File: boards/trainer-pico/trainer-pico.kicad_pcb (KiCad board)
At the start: 2 copper layers, 132.1 x 99.1 mm, 38 parts, among them J1 Conn_01x08_Pin, J10 Conn_01x04_Socket, J11 Conn_01x17_Pin, J12 Conn_01x17_Socket, J13 Conn_01x17_Socket, J14 Conn_01x17_Pin, J15 Barrel_Jack_Switch, J16 Conn_01x04_Pin, J17 Conn_01x04_Pin, J18 Conn_01x04_Pin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

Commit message: 改番
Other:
- board text added: "trainer-pico v1.1"
- board text removed: "trainer-pico v1.0"
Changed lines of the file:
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@@
 		)
 	)
-	(gr_text "trainer-pico v1.0"
+	(gr_text "trainer-pico v1.1"
 		(at 63.5 144.78 0)
 		(layer "F.SilkS")

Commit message: 配置の修正とピンアサインの刻印の追加
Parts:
- moved J10 7.62 mm to (119.4, 111.8)
- moved J5 7.62 mm to (111.8, 111.8)
- moved J4 5.08 mm to (111.8, 96.5)
- moved J9 5.08 mm to (119.4, 96.5)
- moved J3 2.54 mm to (111.8, 76.2)
- moved J8 2.54 mm to (119.4, 76.2)
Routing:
- net /UART_PICO_RX: track 63.1 -> 56.9 mm
- net /UART_PICO_TX: track 63.1 -> 56.9 mm
- net /I2C_SCL: track 74.1 -> 69.8 mm
- net /I2C_SDA: track 72.3 -> 68.0 mm
- net /SPI_MISO: track 65.6 -> 66.7 mm
- net GND: vias 214 -> 207
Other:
- board text added: "I2C0"
- board text added: "SPI1"
- board text added: "SPI1_MISO - GP8 SPI1_MOSI - GP9 SPI1_SCK - GP10 SPI1_CS - GP11 I2C0_SDA - GP21 I2C0_SCL - GP20 UART0_RX - GP17 UART0_TX - GP16"
- board text added: "UART0"
- board text removed: "I2C"
- board text removed: "SPI"
- board text removed: "UART"

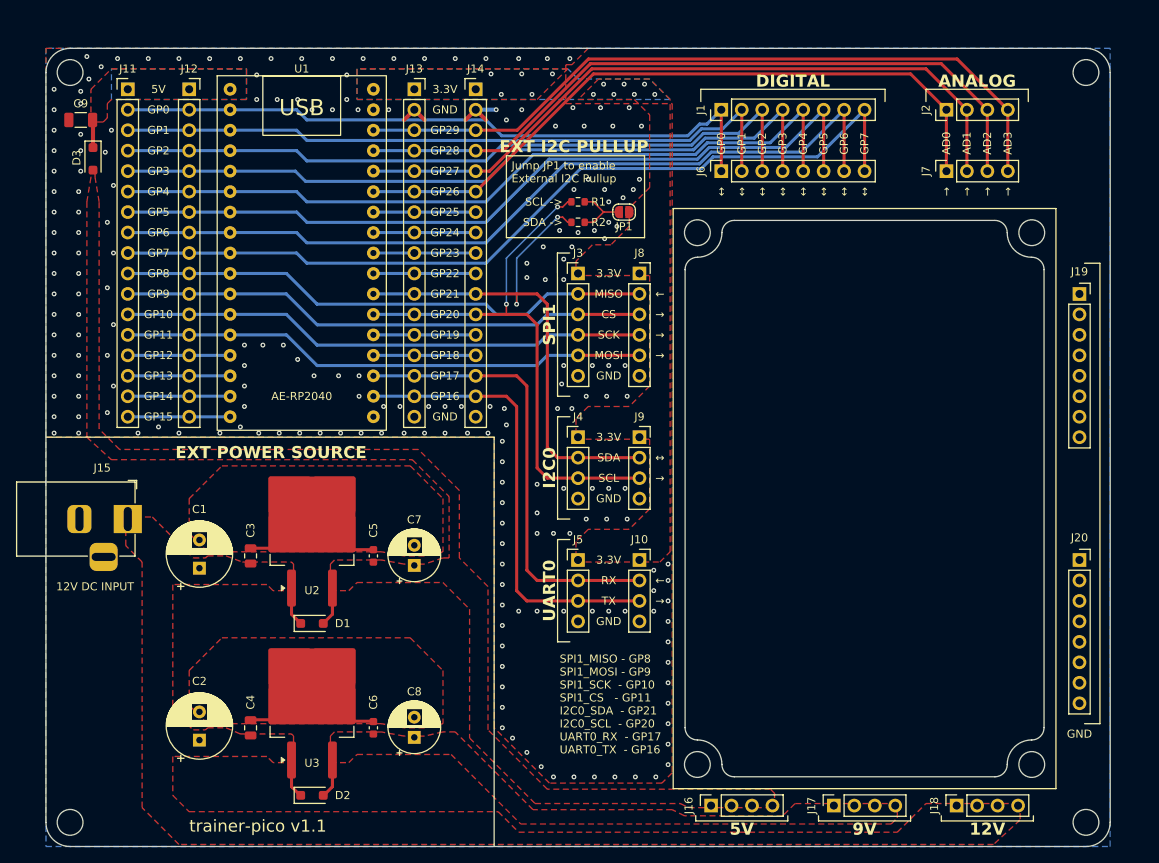
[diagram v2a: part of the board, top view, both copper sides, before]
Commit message: サブ基板の固定方法を変更
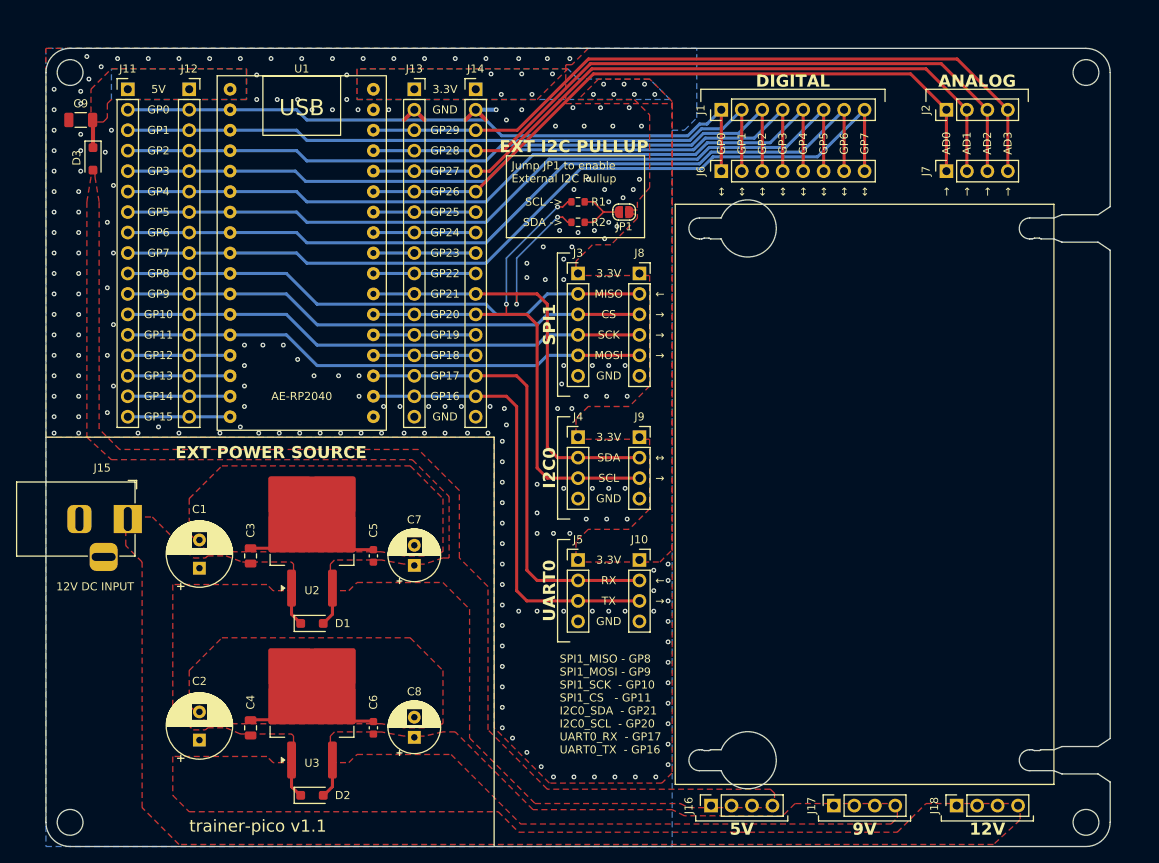
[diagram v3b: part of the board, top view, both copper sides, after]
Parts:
- removed J19, J20: Conn_01x08_Pin, Connector_PinSocket_2.54mm:PinSocket_1x08_P2.54mm_Vertical
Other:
- outline, holes or cut-outs redrawn

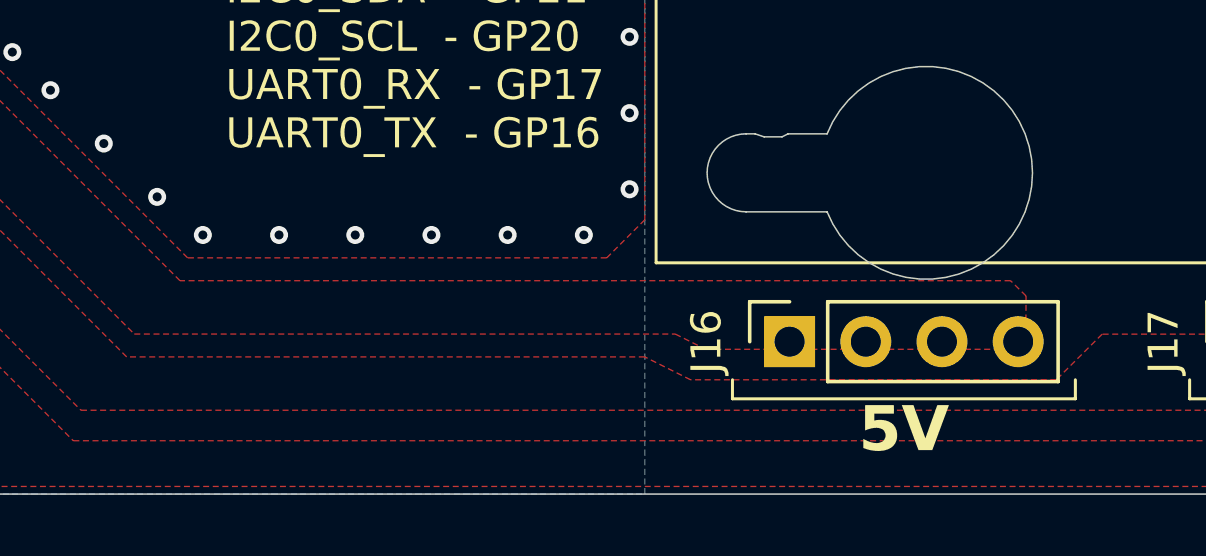
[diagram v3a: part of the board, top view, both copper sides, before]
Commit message: ベタ形状変更
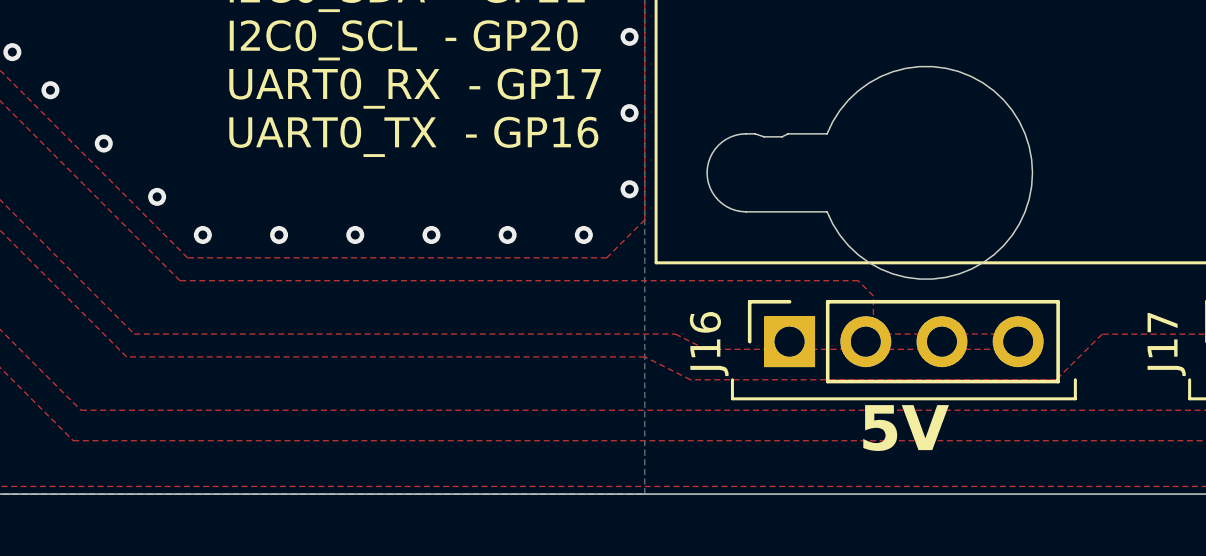
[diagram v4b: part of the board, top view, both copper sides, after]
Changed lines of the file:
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@@
-		(polygon
-			(pts
-				(xy 133.604 140.97) (xy 133.604 141.986) (xy 135.636 141.986) (xy 135.636 140.97)
-			)
-		)
-	)
-	(zone
-		(net 0)
-		(net_name "")
-		(layer "F.Cu")
-		(hatch edge 0.5)
-		(connect_pads
-			(clearance 0)
-		)
-		(min_thickness 0.25)
-		(filled_areas_thickness no)
-		(keepout
-			(tracks allowed)
-			(vias allowed)
-			(pads allowed)
-			(copperpour not_allowed)
-			(footprints allowed)
-		)
-		(fill
-			(thermal_gap 0.5)
-			(thermal_bridge_width 0.5)
-		)
 		(polygon
 			(pts
@@
 				(xy 81.026 115.57) (xy 83.312 115.57) (xy 84.328 114.554) (xy 94.996 114.554) (xy 98.298 117.856)
 				(xy 98.298 133.858) (xy 106.426 141.986) (xy 124.46 141.986) (xy 125.476 142.494) (xy 136.144 142.494)
-				(xy 136.152 140.716) (xy 135.636 140.208) (xy 107.95 140.208) (xy 100.584 132.842) (xy 100.584 115.062)
-				(xy 97.028 111.506) (xy 97.028 103.124) (xy 91.948 98.044) (xy 54.864 98.044) (xy 52.324 95.504)
-				(xy 52.324 67.31) (xy 51.816 64.262) (xy 51.816 63.633) (xy 51.816 63.004) (xy 51.308 63.004) (xy 51.308 64.262)
-				(xy 50.8 67.31) (xy 50.8 96.52) (xy 53.848 99.314) (xy 91.186 99.314) (xy 95.758 103.886) (xy 95.758 111.506)
-				(xy 94.996 111.506) (xy 92.71 112.268) (xy 90.17 112.268) (xy 87.376 111.76) (xy 81.534 111.76)
-				(xy 81.026 112.268)
+				(xy 136.144 141.986) (xy 131.064 141.986) (xy 131.064 140.716) (xy 130.556 140.208) (xy 107.95 140.208)
+				(xy 100.584 132.842) (xy 100.584 115.062) (xy 97.028 111.506) (xy 97.028 103.124) (xy 91.948 98.044)
+				(xy 54.864 98.044) (xy 52.324 95.504) (xy 52.324 67.31) (xy 51.816 64.262) (xy 51.816 63.633) (xy 51.816 63.004)
+				(xy 51.308 63.004) (xy 51.308 64.262) (xy 50.8 67.31) (xy 50.8 96.52) (xy 53.848 99.314) (xy 91.186 99.314)
+				(xy 95.758 103.886) (xy 95.758 111.506) (xy 94.996 111.506) (xy 92.71 112.268) (xy 90.17 112.268)
+				(xy 87.376 111.76) (xy 81.534 111.76) (xy 81.026 112.268)
 			)
 		)
@@
 		(polygon
 			(pts
-				(xy 131.064 140.97) (xy 131.064 141.986) (xy 133.096 141.986) (xy 133.096 140.97)
-			)
-		)
-	)
-	(zone
-		(net 0)
-		(net_name "")
-		(layer "F.Cu")
-		(hatch edge 0.5)
-		(connect_pads
-			(clearance 0)
-		)
-		(min_thickness 0.25)
-		(filled_areas_thickness no)
-		(keepout
-			(tracks allowed)
-			(vias allowed)
-			(pads allowed)
-			(copperpour not_allowed)
-			(footprints allowed)
-		)
-		(fill
-			(thermal_gap 0.5)
-			(thermal_bridge_width 0.5)
-		)
-		(polygon
-			(pts
 				(xy 111.252 93.726) (xy 109.22 93.726) (xy 108.458 92.964) (xy 108.458 97.536) (xy 109.474 98.552)
 				(xy 110.49 98.552) (xy 110.49 103.886) (xy 113.03 103.886) (xy 113.03 96.774) (xy 111.252 96.774)
@@
 			)
 		)
-	)
-	(zone
-		(net 0)
-		(net_name "")
-		(layers "F&B.Cu" "Edge.Cuts")
-		(hatch edge 0.5)
-		(connect_pads
-			(clearance 0)
-		)
-		(min_thickness 0.25)
-		(filled_areas_thickness no)
-		(keepout
-			(tracks allowed)
-			(vias allowed)
-			(pads allowed)
-			(copperpour not_allowed)
-			(footprints allowed)
-		)
-		(fill
-			(thermal_gap 0.5)
-			(thermal_bridge_width 0.5)
-		)
-		(polygon
-			(pts
-				(xy 170.82 139.612) (xy 170.82 67.612) (xy 123.82 67.612) (xy 123.82 139.612)
-			)
-		)
